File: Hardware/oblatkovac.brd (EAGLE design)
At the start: 110 x 75 mm, 42 parts, among them SW1 EC12E_SW, T1 2N2222, X1 ~230V

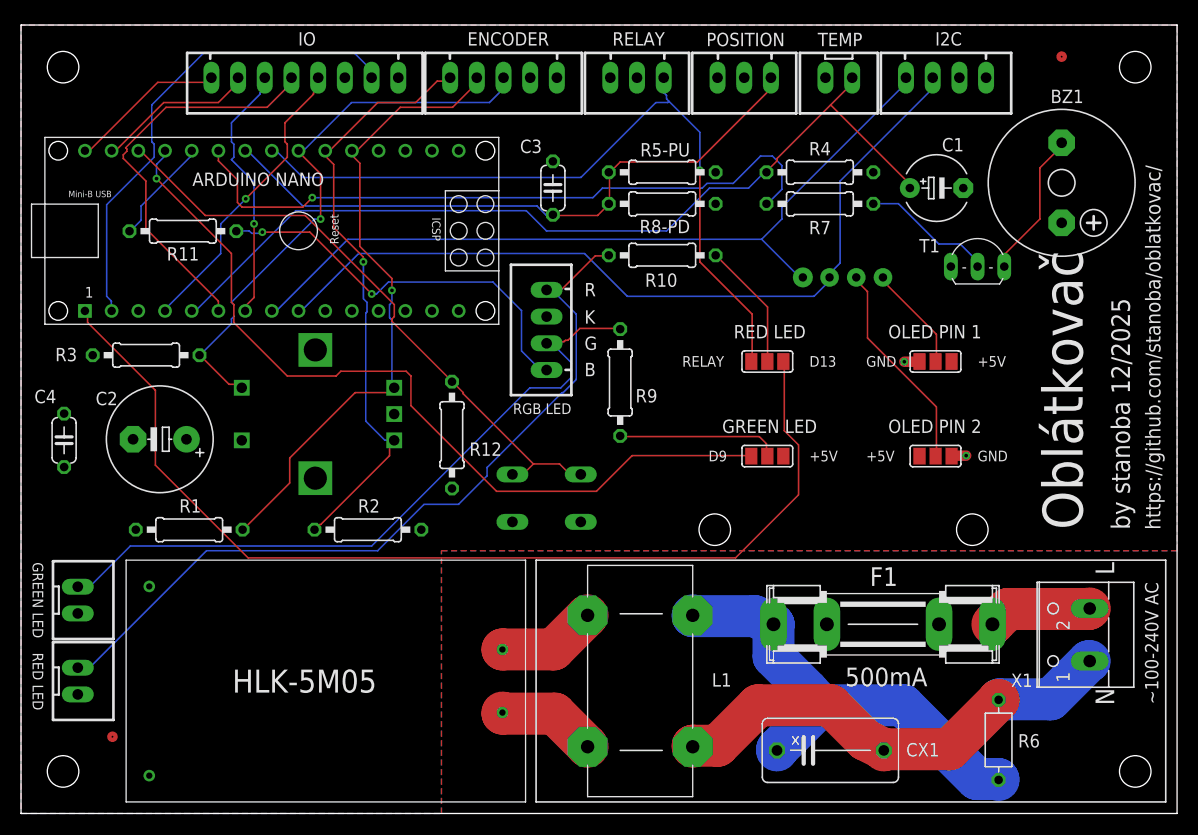
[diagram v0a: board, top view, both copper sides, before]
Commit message: - Improved temperature sensing, heater control, and UI. - Integrated EEPROM for saving settings. - Configured button handlers for menu navigation and start/stop functionality. - Established pin definitions for various components including relay, buzzer, and LEDs. - Updated README.md files - Reorganized folder structure - Added 3D models
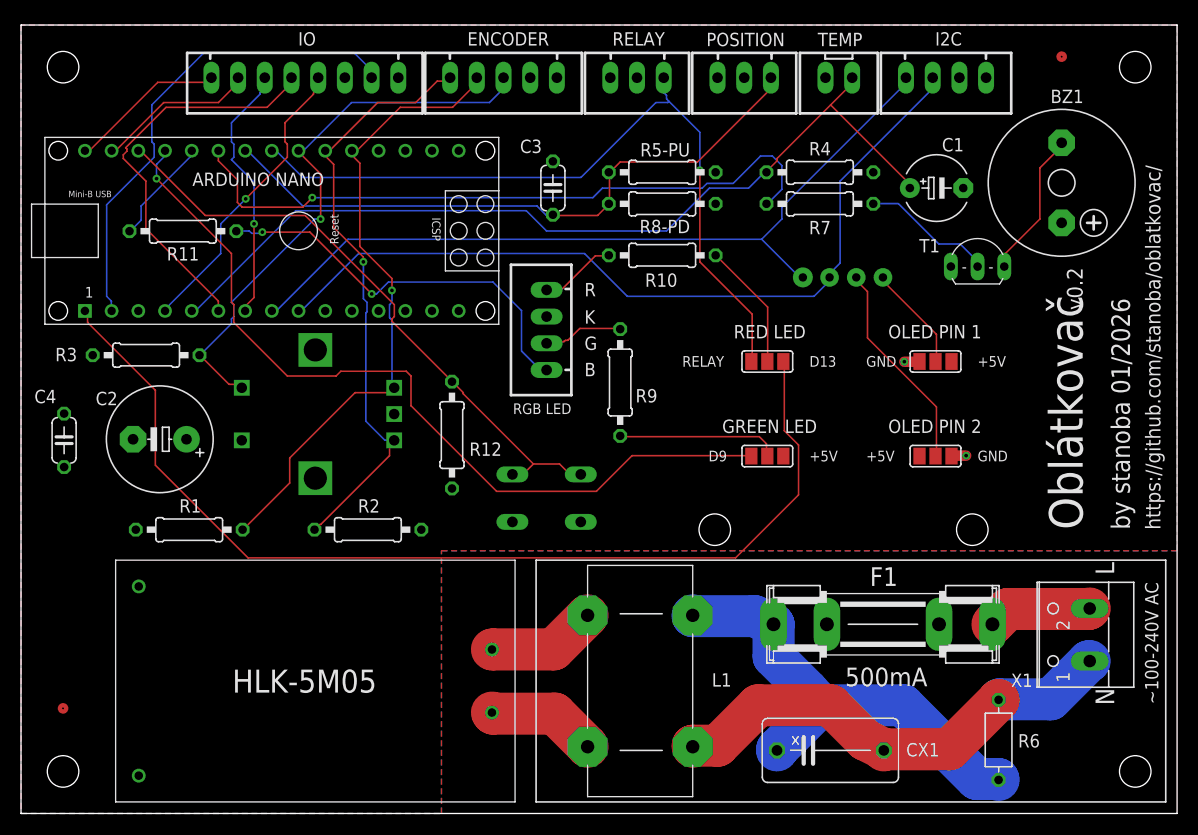
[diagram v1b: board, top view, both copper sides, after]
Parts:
- removed LED1: CN9, Rembrandt Electronics - JST XH Connectors v1-0:JST-XH-02-PACKAGE-LONG-PAD
- removed LED2: CN8, Rembrandt Electronics - JST XH Connectors v1-0:JST-XH-02-PACKAGE-LONG-PAD
- R10, R11: value 150 -> 4k7
- R9: value 150 -> 10k
- moved U$3 5.42 mm to (4.00, 10.0)
- moved U$2 1.00 mm to (47.0, 24.1)
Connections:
- net GND: no longer LED1.2, LED2.2
- net N$5: no longer LED2.1
- net N$6: no longer LED1.1
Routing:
- net N$6: track 76.5 -> 7.28 mm
- net N$5: track 67.3 -> 7.59 mm
- net LIVE_FUSED3: track 9.45 -> 10.4 mm
- net NEUTRAL2: track 9.51 -> 10.5 mm
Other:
- board text added: "by stanoba 01/2026"
- board text added: "v0.2"
- board text removed: "A"
- board text removed: "by stanoba 12/2025"
